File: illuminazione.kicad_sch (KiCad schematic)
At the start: 20 parts, among them J1 Interior LEDs, J2 PowerIn, J7 Exterior LEDs, Q1 IRLB8721PBF, Q2 IRLB8721PBF, Q3 IRLB8721PBF, SW2 SW_DIP_x01, U5 AP2112K-3.3

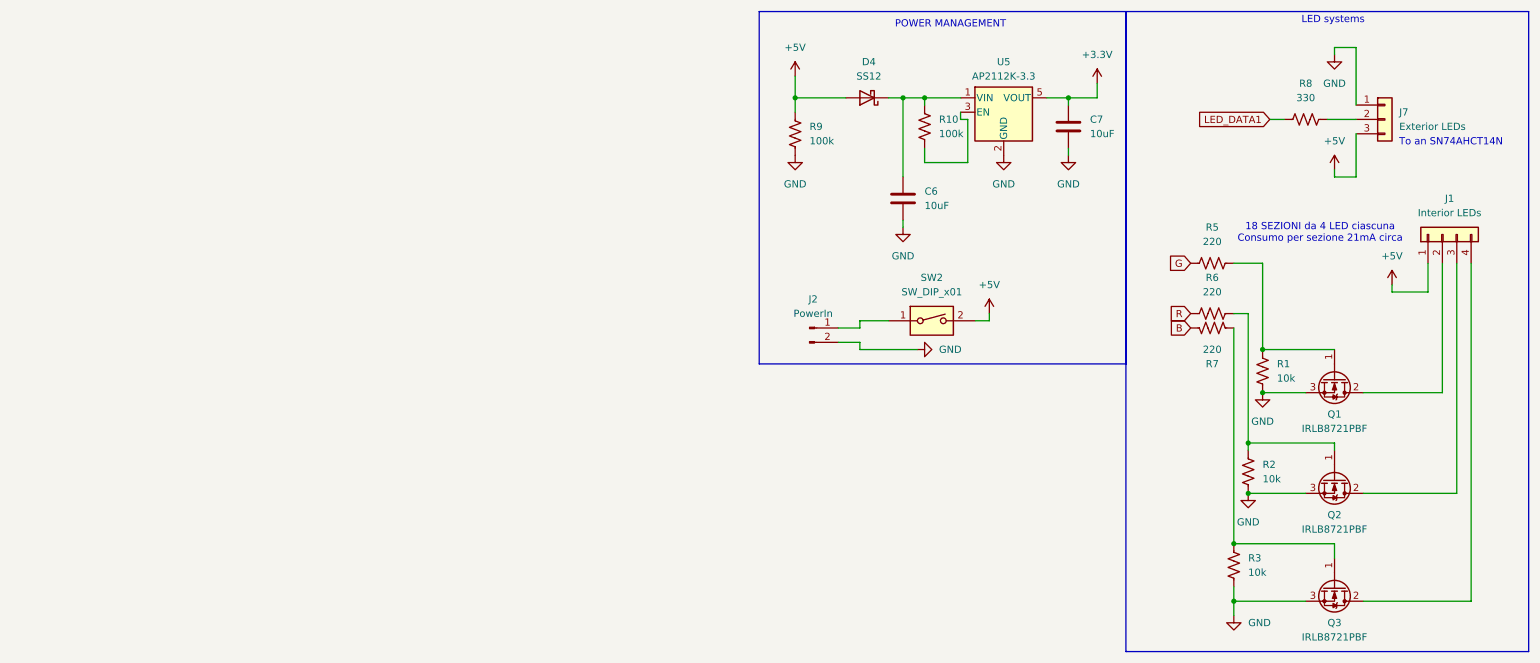
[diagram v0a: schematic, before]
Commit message: Ligthing schematic update
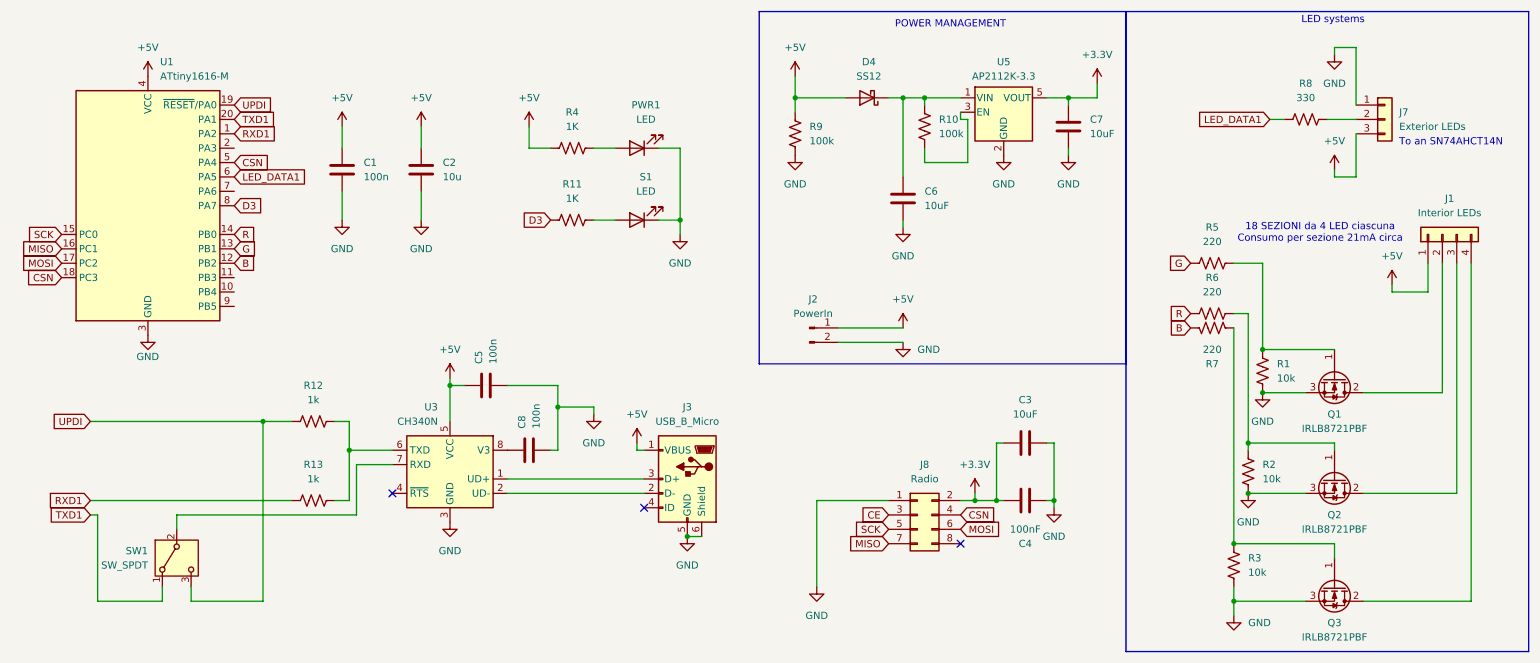
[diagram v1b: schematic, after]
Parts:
- removed SW2: SW_DIP_x01, Connector_PinHeader_2.54mm:PinHeader_1x02_P2.54mm_Vertical, symbol Switch:SW_DIP_x01
- added C1, C5, C8: 100n, Capacitor_SMD:C_0402_1005Metric_Pad0.74x0.62mm_HandSolder, symbol Device:C
- added C2: 10u, Capacitor_SMD:C_0402_1005Metric_Pad0.74x0.62mm_HandSolder, symbol Device:C
- added C3: 10uF, Capacitor_SMD:C_0402_1005Metric_Pad0.74x0.62mm_HandSolder, symbol Device:C
- added C4: 100nF, Capacitor_SMD:C_0402_1005Metric_Pad0.74x0.62mm_HandSolder, symbol Device:C
- added J3: USB_B_Micro, Connector_USB:USB_Micro-B_Amphenol_10118194-0001LF_Horizontal, symbol Connector:USB_B_Micro
- added J8: Radio, Connector_PinHeader_2.54mm:PinHeader_2x04_P2.54mm_Vertical, symbol Connector_Generic:Conn_02x04_Odd_Even
- added PWR1, S1: LED, LED_SMD:LED_0402_1005Metric_Pad0.77x0.64mm_HandSolder, symbol Device:LED
- added R11, R4: 1K, Resistor_SMD:R_0402_1005Metric_Pad0.72x0.64mm_HandSolder, symbol Device:R_US
- added R12, R13: 1k, Resistor_SMD:R_0402_1005Metric_Pad0.72x0.64mm_HandSolder, symbol Device:R_US
- added SW1: SW_SPDT, Button_Switch_SMD:SW_SPDT_CK_JS102011SAQN, symbol Switch:SW_SPDT
- added U1: ATtiny1616-M, Package_DFN_QFN:VQFN-20-1EP_3x3mm_P0.4mm_EP1.7x1.7mm, symbol MCU_Microchip_ATtiny:ATtiny1616-M
- added U3: CH340N, Package_SO:SOP-8_3.9x4.9mm_P1.27mm, symbol Interface_USB:CH340N
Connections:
- net +3.3V: now also C3.1, C4.2, J8.2 (Pin_2)
- net +5V: now also J2.1 (Pin_1), C1.1, C2.1, C5.1, J3.1 (VBUS), R4.1, U1.4 (VCC), U3.5 (VCC)
- net B: now also U1.12 (PB2)
- net G: now also U1.13 (PB1)
- net GND: now also C1.2, C2.2, C3.2, C4.1, C5.2, C8.2, J3.5 (GND), J3.6 (Shield), J8.1 (Pin_1), PWR1.1 (K), S1.1 (K), U1.21 (GND), U1.3 (GND), U3.3 (GND)
- net LED_DATA1: now also U1.6 (PA5)
- net R: now also U1.14 (PB0)
- new net: SW1.2 (B), U3.7 (RXD)
- new net: R12.2, R13.2, U3.6 (TXD)
- new net: R11.2, S1.2 (A)
- new net: J3.3 (D+), U3.1 (UD+)
- new net: J3.2 (D-), U3.2 (UD-)
- new net: C8.1, U3.8 (V3)
- new net: PWR1.2 (A), R4.2
- new net CE: J8.3 (Pin_3)
- new net CSN: J8.4 (Pin_4), U1.18 (PC3), U1.5 (PA4)
- new net D3: R11.1, U1.8 (PA7)
- new net MISO: J8.7 (Pin_7), U1.16 (PC1)
- new net MOSI: J8.6 (Pin_6), U1.17 (PC2)
- new net RXD1: R13.1, U1.1 (PA2)
- new net SCK: J8.5 (Pin_5), U1.15 (PC0)
- new net TXD1: SW1.1 (A), U1.20 (PA1)
- new net UPDI: R12.1, SW1.3 (C), U1.19 (~{RESET}/PA0)
- no-connect marks 0 -> 3

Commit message: General Changes
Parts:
- removed C3, C6, C7: 10uF, Capacitor_SMD:C_0402_1005Metric_Pad0.74x0.62mm_HandSolder, symbol Device:C
- removed C4: 100nF, Capacitor_SMD:C_0402_1005Metric_Pad0.74x0.62mm_HandSolder, symbol Device:C
- removed C5, C8: 100n, Capacitor_SMD:C_0402_1005Metric_Pad0.74x0.62mm_HandSolder, symbol Device:C
- removed D4: SS12, Diode_SMD:D_SMA, symbol Diode:SS12
- removed J3: USB_B_Micro, Connector_USB:USB_Micro-B_Amphenol_10118194-0001LF_Horizontal, symbol Connector:USB_B_Micro
- removed J8: Radio, Connector_PinHeader_2.54mm:PinHeader_2x04_P2.54mm_Vertical, symbol Connector_Generic:Conn_02x04_Odd_Even
- removed R12, R13: 1k, Resistor_SMD:R_0402_1005Metric_Pad0.72x0.64mm_HandSolder, symbol Device:R_US
- removed SW1: SW_SPDT, Button_Switch_SMD:SW_SPDT_CK_JS102011SAQN, symbol Switch:SW_SPDT
- removed U3: CH340N, Package_SO:SOP-8_3.9x4.9mm_P1.27mm, symbol Interface_USB:CH340N
- removed U5: AP2112K-3.3, Package_TO_SOT_SMD:SOT-23-5, symbol Regulator_Linear:AP2112K-3.3
- added C11: 10u, Capacitor_SMD:C_0402_1005Metric_Pad0.74x0.62mm_HandSolder, symbol Device:C
- added C12: 100n, Capacitor_SMD:C_0402_1005Metric_Pad0.74x0.62mm_HandSolder, symbol Device:C
- added D129: SM712_SOT23, Package_TO_SOT_SMD:SOT-23, symbol Diode:SM712_SOT23
- added J3: UDPI, symbol Connector:Conn_01x03_Pin
- added J4: RS485, Connector_JST:JST_NV_B02P-NV_1x02_P5.00mm_Vertical, symbol Connector:Conn_01x02_Pin
- added U10: THVD1450DR, Package_SON:VSON-8-1EP_3x3mm_P0.65mm_EP1.6x2.4mm, symbol Interface_UART:THVD1450DR
- R10, R9: value 100k -> 10k
- U1: value ATtiny1616-M -> ATtiny1626-M; symbol MCU_Microchip_ATtiny:ATtiny1616-M -> MCU_Microchip_ATtiny:ATtiny1626-M
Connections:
- net +5V: now also C11.1, C12.1, J3.3 (Pin_3), U10.8 (VCC)
- net GND: now also R10.2, C11.2, C12.2, D129.3 (common), J3.1 (Pin_1), U10.5 (GND); no longer R9.2
- net D9: now reaches R10.1
- net D9: now also R9.2, U10.2 (~{RE}), U10.3 (DE)
- net CSN: no longer names the net of U1.18 (PC3)
- net CSN: no longer U1.5 (PA4)
- net MISO: no longer names the net of U1.16 (PC1)
- net MOSI: no longer names the net of U1.17 (PC2)
- net RXD1 renamed RXD2
- net RXD2: now also U10.1 (RO)
- net SCK: no longer names the net of U1.15 (PC0)
- net TXD1 renamed TXD2
- net TXD2: now also U10.4 (DI)
- net UPDI: no longer names the net of U1.19 (~{RESET}/PA0)
- net UPDI: now also J3.2 (Pin_2)
- new net: D129.1 (A1), J4.2 (Pin_2), U10.6 (A)
- new net: D129.2 (A2), J4.1 (Pin_1), U10.7 (B)
- no-connect marks 3 -> 0
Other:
- moved on the sheet: C1, C2, J2, PWR1, R11, R4, S1
